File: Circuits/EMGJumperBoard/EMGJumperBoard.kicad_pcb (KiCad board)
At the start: 2 copper layers, 2 parts

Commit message: Further work on the xfer board
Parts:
- moved Omnetics1 32.1 mm to (116.2, 56.4)
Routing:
- net (no net): track 0.00 -> 4116.3 mm, vias 0 -> 1800
- net Net-(Omnetics1-Pad20): track 24.8 -> 0.00 mm
- net Net-(Omnetics1-Pad22): track 23.0 -> 0.00 mm
- net Net-(Omnetics1-Pad24): track 22.8 -> 0.00 mm
- net Net-(Omnetics1-Pad26): track 21.6 -> 0.00 mm
- net Net-(Omnetics1-Pad28): track 19.3 -> 0.00 mm
- net Net-(Omnetics1-Pad30): track 17.3 -> 0.00 mm
- net Net-(Omnetics1-Pad32): track 17.0 -> 0.00 mm
- net Net-(Omnetics1-Pad34): track 16.8 -> 0.00 mm
- net Net-(Omnetics1-Pad36): track 16.4 -> 0.00 mm
- net Net-(Omnetics1-Pad35): track 15.9 -> 0.00 mm
- net Net-(Omnetics1-Pad17): track 5.61 -> 0.00 mm, vias 1 -> 0
- net Net-(Omnetics1-Pad19): track 5.61 -> 7.95 mm, vias 1 -> 0
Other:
- board outline added: 50.8 x 63.5 mm
- net class Default: clearance 0.2 -> 0.1524; trace_width 0.2 -> 0.1524; via_dia 0.6 -> 0.508; via_drill 0.4 -> 0.254
- net class OSHPark: via_dia 0.381 -> 0.508
- rule trace_clearance: 0.2 -> 0.1524
- rule via_min_size: 0.3 -> 0.508

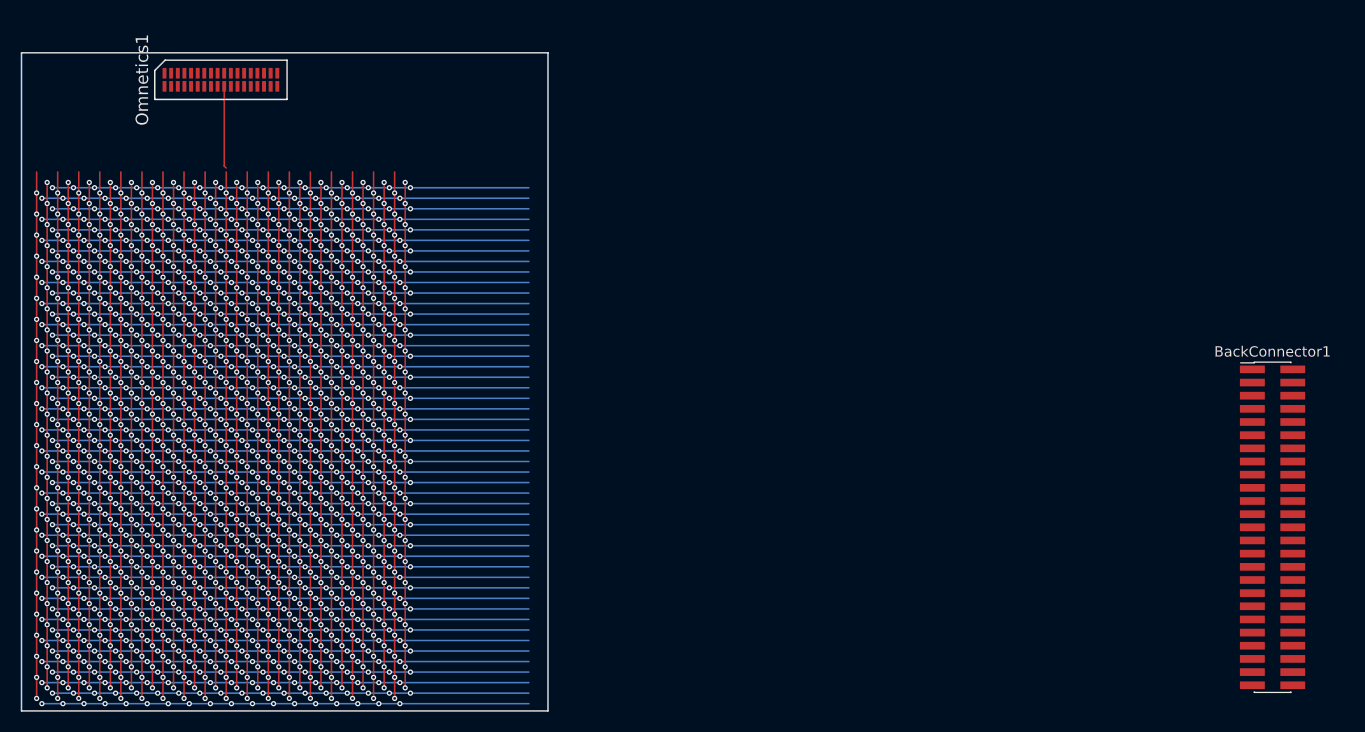
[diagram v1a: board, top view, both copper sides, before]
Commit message: Some updates to jPCA code so that it works with Chethan's, and 	work on new EMG board -- the smaller(ish) version
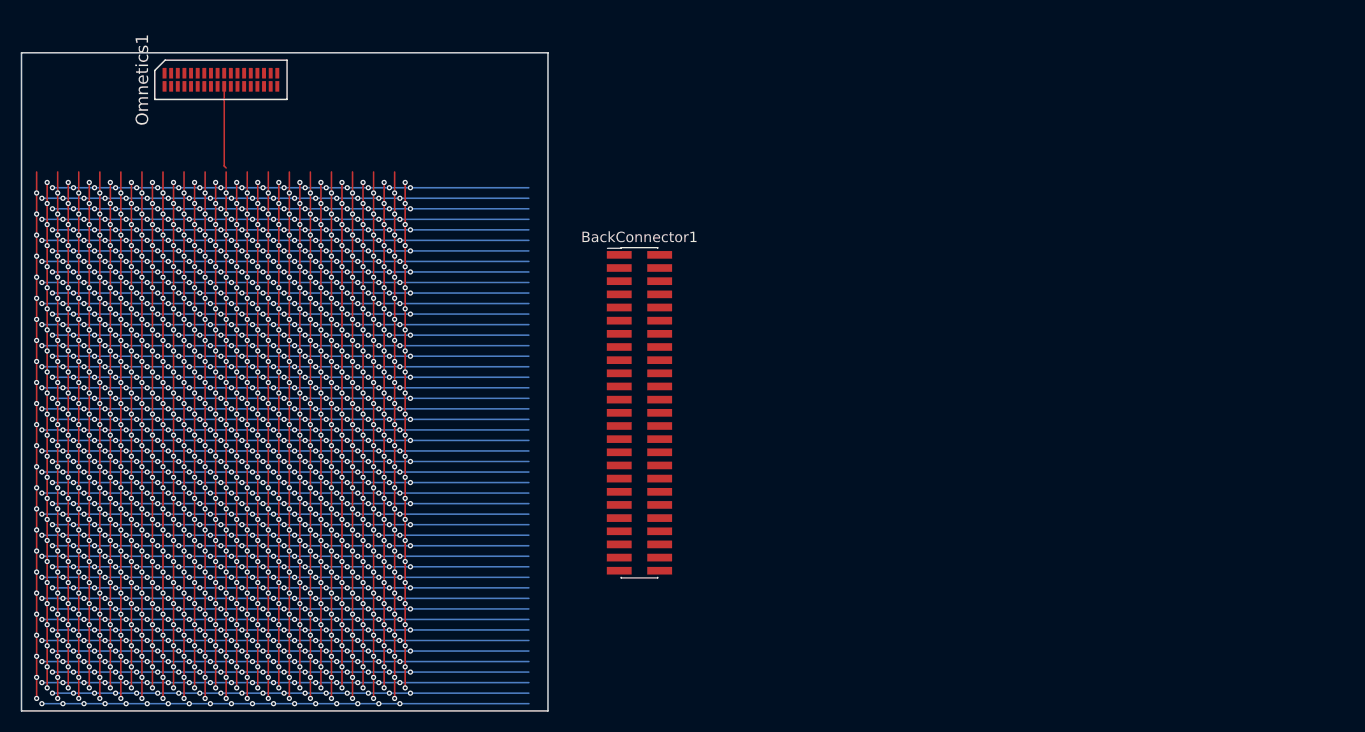
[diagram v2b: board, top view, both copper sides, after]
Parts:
- moved BackConnector1 62.1 mm to (156.6, 88.5)
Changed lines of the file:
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@@
   )
   (module Pin_Headers:Pin_Header_Straight_2x25_Pitch1.27mm_SMD (layer F.Cu)
-    (at 217.678 99.568)
+    (at 156.591 88.519)
     (descr "surface-mounted straight pin header, 2x25, 1.27mm pitch, double rows")
     (tags "Surface mounted pin header SMD 2x25 1.27mm double row")
@@
   (segment (start 99.441 70.358) (end 99.441 68.326) (width 0.1524) (layer F.Cu) (net 0))
   (segment (start 99.441 68.326) (end 99.441 66.294) (width 0.1524) (layer F.Cu) (net 0))
-  (segment (start 116.525 57.023) (end 116.525 64.709) (width 0.1524) (layer F.Cu) (net 70) (status 400000))
+  (segment (start 116.525 57.023) (end 116.525 64.709) (width 0.1524) (layer F.Cu) (net 70))
   (segment (start 116.525 64.709) (end 116.713 64.897) (width 0.1524) (layer F.Cu) (net 70))
 )
